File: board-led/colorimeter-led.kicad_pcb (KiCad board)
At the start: 2 copper layers, 23.5 x 8.9 mm, 2 parts, among them J1 Conn_02x03_Odd_Even

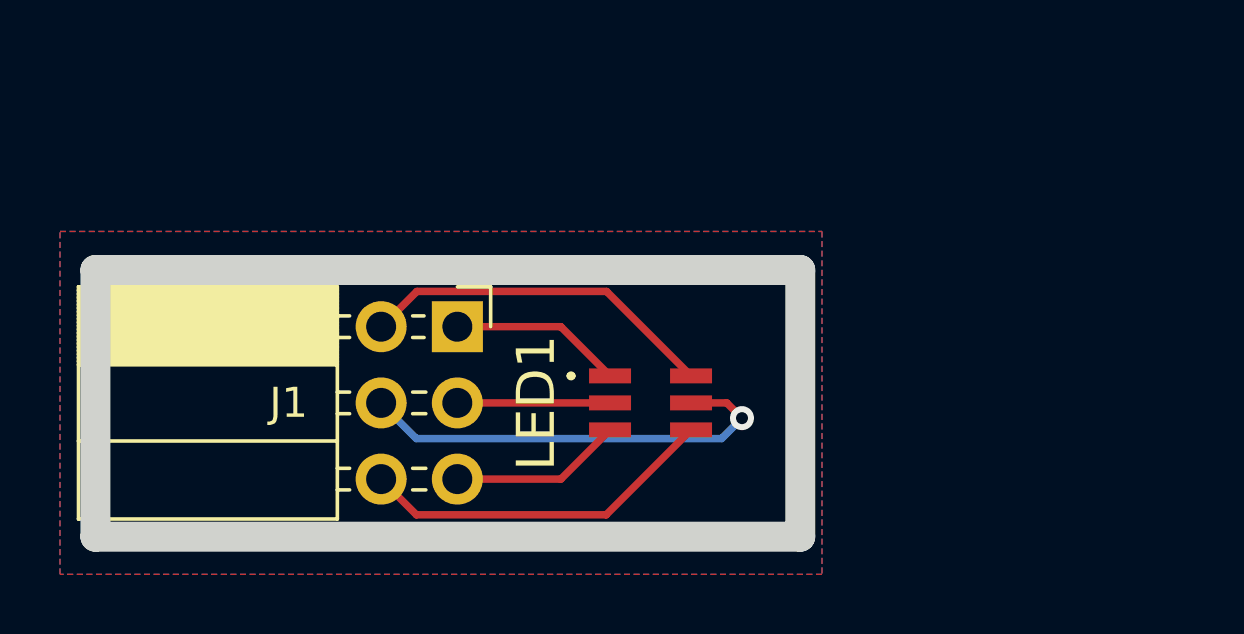
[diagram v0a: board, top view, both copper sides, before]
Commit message: Change PD, LED boards to match pinout on main board
Added ground connections to both
Changed Photodiode to have 3x2 connector
Changed LED to common anode
Added new symbol & footprint for common anode RGB LED

Signed-off-by: Ioan Dragomir <ioan.dragomir@analog.com>
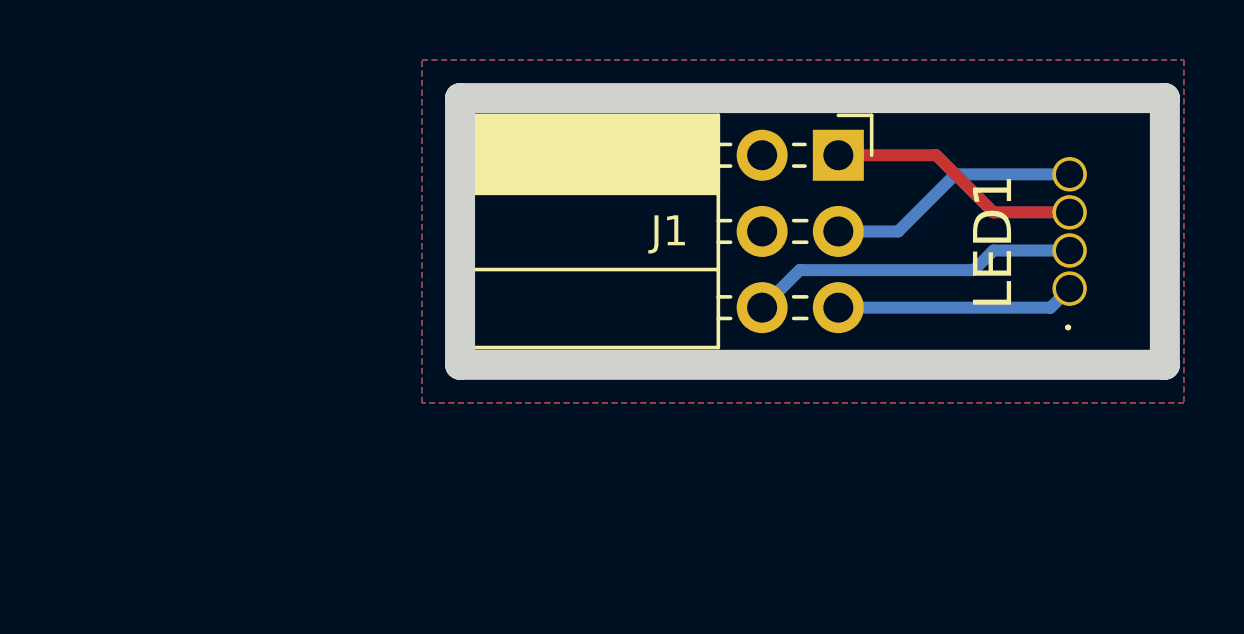
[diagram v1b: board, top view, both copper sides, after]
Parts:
- LED1: value ASMB-UTF0-0D20B -> 521-8559F; footprint footprints:ASMBUTF00D20B -> footprints:5218559F
- moved LED1 14.5 mm to (109.2, 69.8), turned to 180 degrees
- moved J1 13.9 mm to (101.5, 65.4)
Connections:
- J1 pad 1: Net-(J1-Pin_1) -> /B
- J1 pad 2: Net-(J1-Pin_2) -> GND
- J1 pad 3: Net-(J1-Pin_3) -> /G
- J1 pad 4: Net-(J1-Pin_4) -> GND
- J1 pad 5: Net-(J1-Pin_5) -> /R
- J1 pad 6: Net-(J1-Pin_6) -> /A
- LED1 pad 1: Net-(J1-Pin_1) -> /R
- LED1 pad 2: Net-(J1-Pin_2) -> /A
- LED1 pad 3: Net-(J1-Pin_3) -> /B
- LED1 pad 4: Net-(J1-Pin_4) -> /G
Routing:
- net Net-(J1-Pin_4): track 14.7 -> 0.00 mm, vias 1 -> 0
- net Net-(J1-Pin_2): track 12.6 -> 0.00 mm
- net Net-(J1-Pin_6): track 12.0 -> 0.00 mm
- net /A: track 0.00 -> 11.0 mm
- net /B: track 0.00 -> 8.50 mm
- net /G: track 0.00 -> 8.50 mm
- net /R: track 0.00 -> 7.97 mm
- net Net-(J1-Pin_5): track 5.77 -> 0.00 mm
- net Net-(J1-Pin_1): track 5.77 -> 0.00 mm
- net Net-(J1-Pin_3): track 5.09 -> 0.00 mm
- added copper zone on B.Cu, net GND
- added copper zone on F.Cu, net GND
- removed copper zone on B.Cu, net (none)
- removed copper zone on F.Cu, net (none)
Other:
- board text added: "LED Riser v1"
- board text removed: "RGB LED Riser v1"
